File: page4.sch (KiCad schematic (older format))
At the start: 1 part

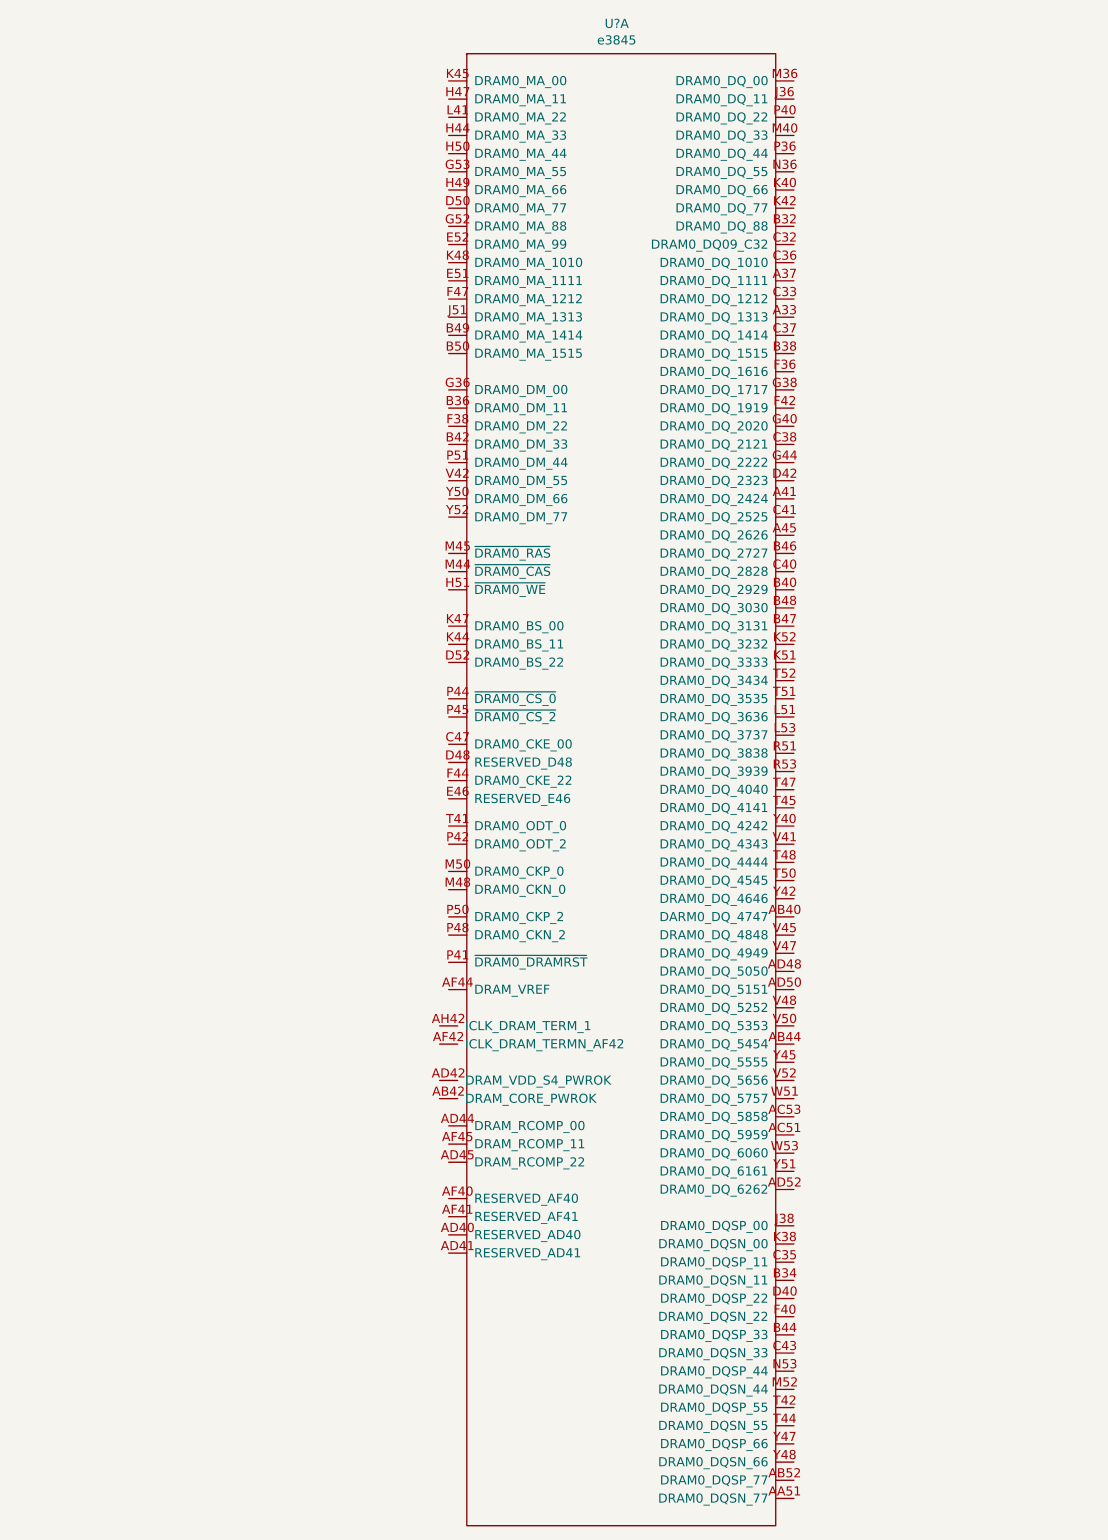
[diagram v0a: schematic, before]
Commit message: Schematic capture update page 5
Schematic capture update page 5
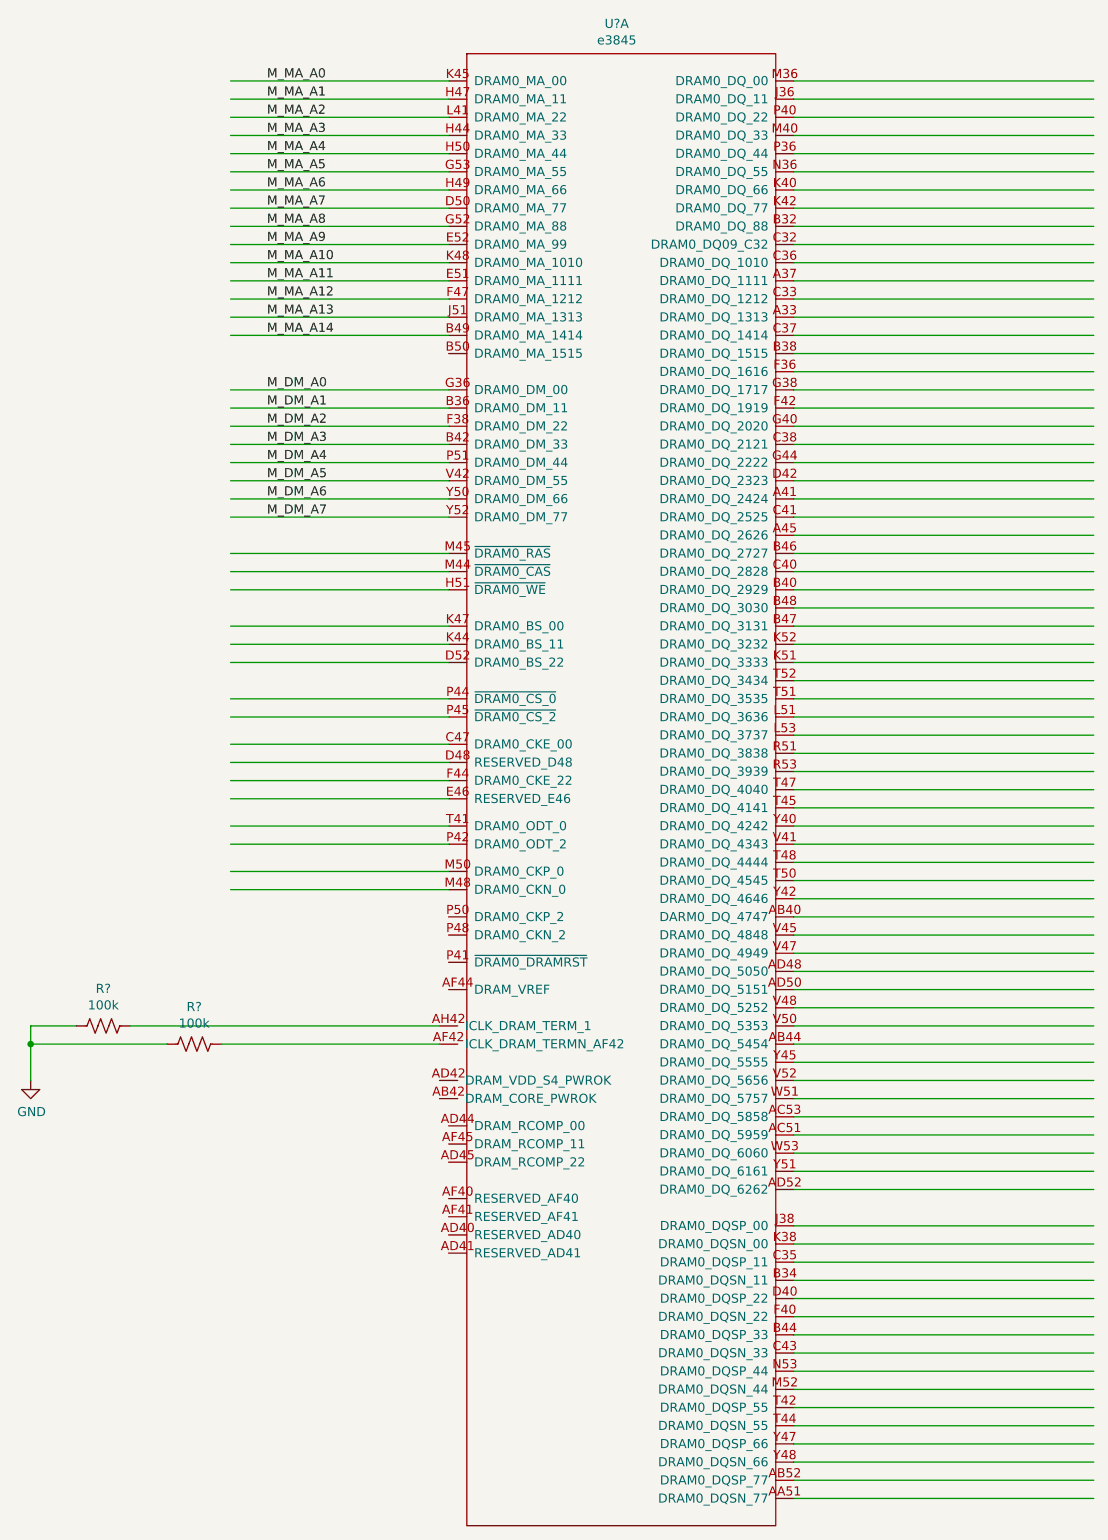
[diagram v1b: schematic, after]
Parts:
- added R? (x2): 100k, symbol Device:R_US
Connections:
- net labels added: GND, M_DM_A0, M_DM_A1, M_DM_A2, M_DM_A3, M_DM_A4, M_DM_A5, M_DM_A6, M_DM_A7, M_MA_A0, M_MA_A1, M_MA_A10, M_MA_A11, M_MA_A12, M_MA_A13, M_MA_A14, M_MA_A2, M_MA_A3, M_MA_A4, M_MA_A5, M_MA_A6, M_MA_A7, M_MA_A8, M_MA_A9
- wire segments 0 -> 123

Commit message: Schematic update page 4
Schematic capture update on page 4.
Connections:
- net labels added: M_CAS_A_L, M_RAS_A_L, M_WE_A_L
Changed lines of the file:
@@
 U 1 1 6001C6F1
 P 5800 6600
+AR Path="/5FB9CACA/6001C6F1" Ref="R?"  Part="1"
+AR Path="/5FB36FCD/6001C6F1" Ref="R?"  Part="1"
 F 0 "R?" V 5595 6600 50  0000 C CNN
 F 1 "100k" V 5686 6600 50  0000 C CNN
@@
 U 1 1 6001C6F7
 P 5300 6500
+AR Path="/5FB9CACA/6001C6F7" Ref="R?"  Part="1"
+AR Path="/5FB36FCD/6001C6F7" Ref="R?"  Part="1"
 F 0 "R?" V 5095 6500 50  0000 C CNN
 F 1 "100k" V 5186 6500 50  0000 C CNN
@@
 Wire Wire Line
 	7200 5750 6000 5750
+Text Label 6200 3900 0    50   ~ 0
+M_RAS_A_L
+Text Label 6200 4000 0    50   ~ 0
+M_CAS_A_L
+Text Label 6200 4100 0    50   ~ 0
+M_WE_A_L
 $EndSCHEMATC
